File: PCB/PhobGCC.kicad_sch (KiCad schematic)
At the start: 46 parts, among them J1 Conn_01x06_Female, J2 Conn_01x04_Female, J3 Conn_01x01_Male, J4 Conn_01x01_Male, J6 10118194-0001LF, SW1 A, SW10 Dup, SW11 Dright, SW12 Ddown, SW2 B, SW3 X, SW4 Y, SW5 Start, SW6 L, SW7 R, SW8 1825027-5, SW9 Dleft, U1 Teensy3.2, U2 2x DRV5053CAQLPGM Hall Effect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, U3 2.5V LDO

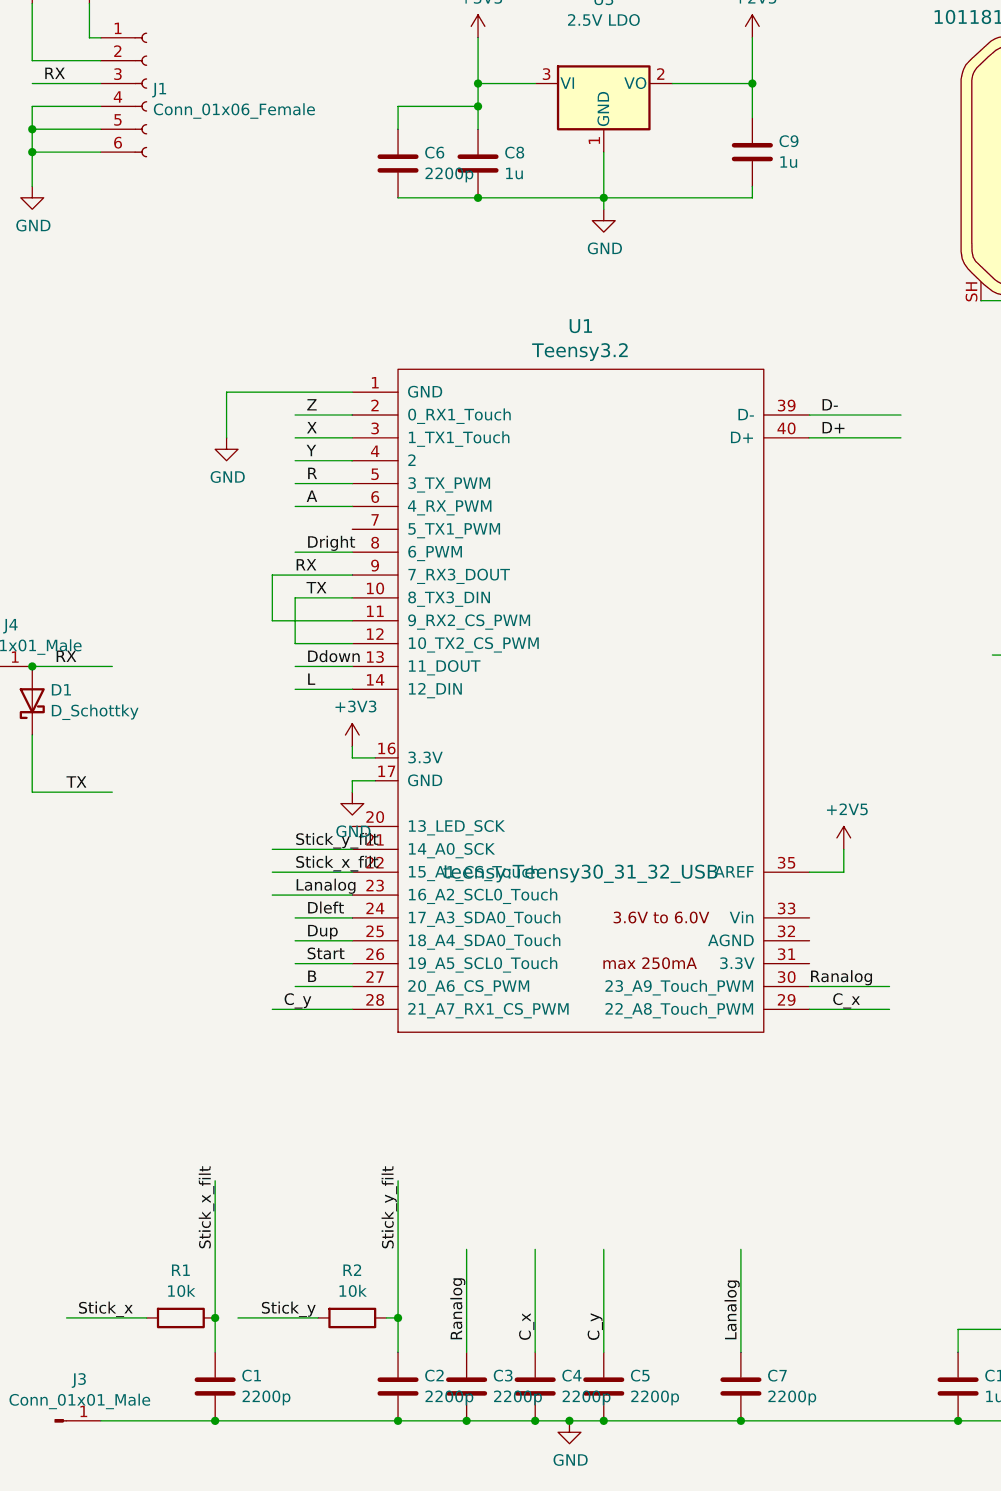
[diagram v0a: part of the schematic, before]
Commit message: Software tweaks to make the 1.1 version board work, and increasing the capacitors on the analog inputs
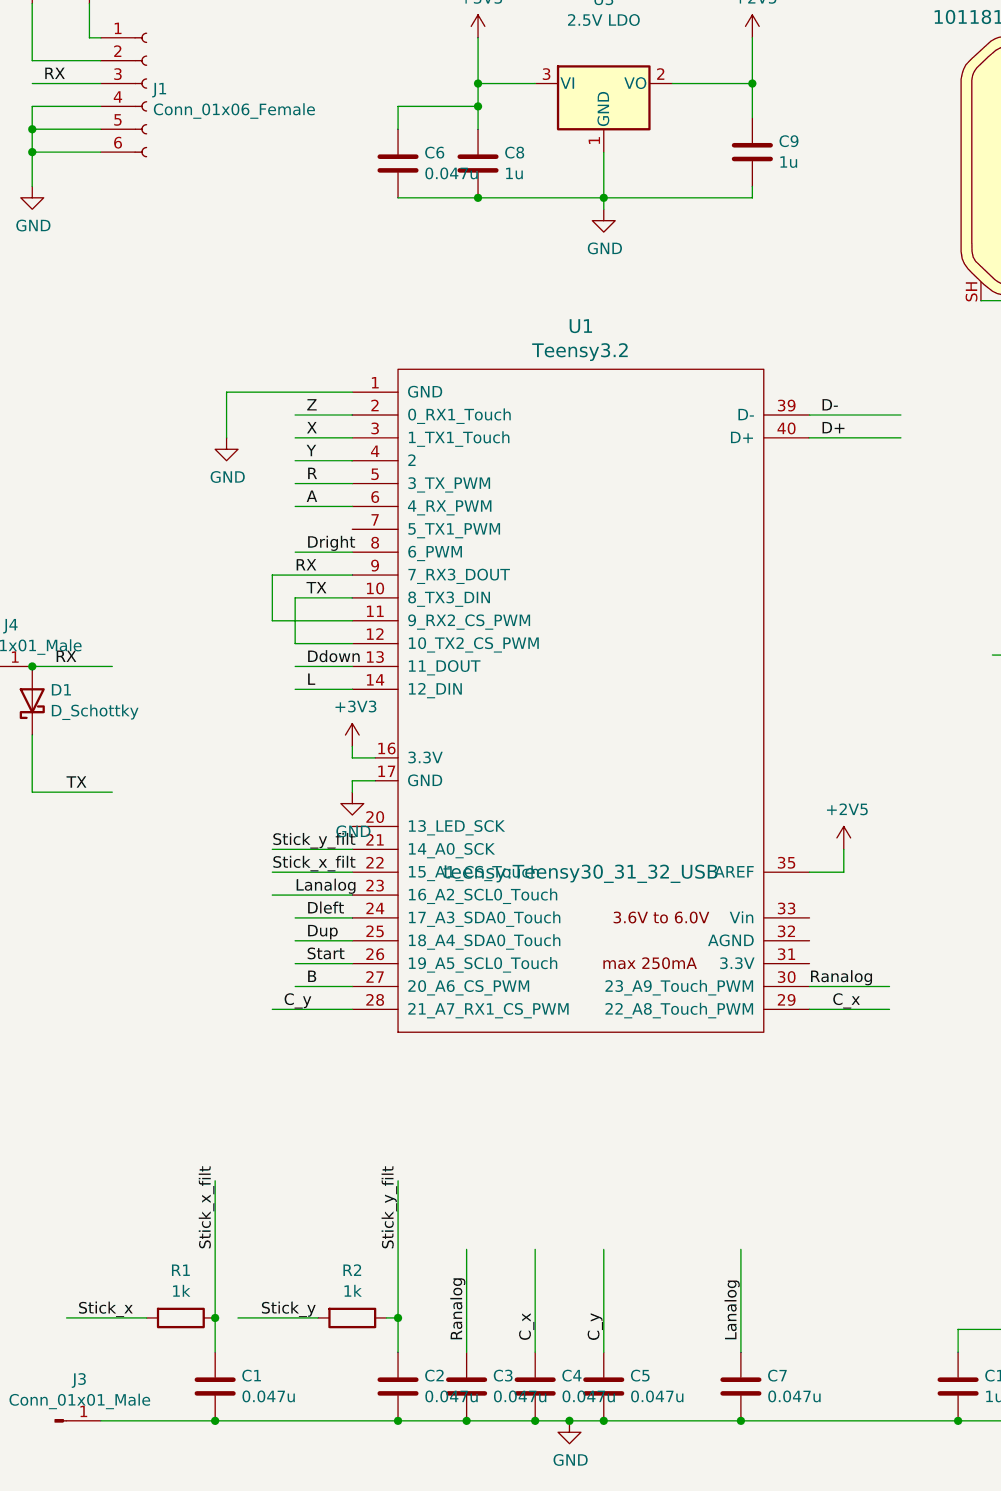
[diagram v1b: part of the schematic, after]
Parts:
- C1, C2, C3, C4, C5, C6, C7: value 2200p -> 0.047u; LCSC C1604 -> (none); MPN 0603B222K500NT -> (none); Manufacturer FH(Guangdong Fenghua Advanced Tech) -> (none)
- R1: value 10k -> 1k; LCSC C25804 -> (none); MPN 0603WAF1002T5E -> (none); Manufacturer UNI-ROYAL -> (none); Manufacturer PN 0603WAF1002T5ECopy -> (none)
- R2: value 10k -> 1k; LCSC C25804 -> (none); MPN 0603WAF1002T5E -> (none); Manufacturer UNI-ROYAL -> (none)

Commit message: Reverted the kicad and gerber files back to the 1.1 board version so they match up with the manufacturing files for JLC
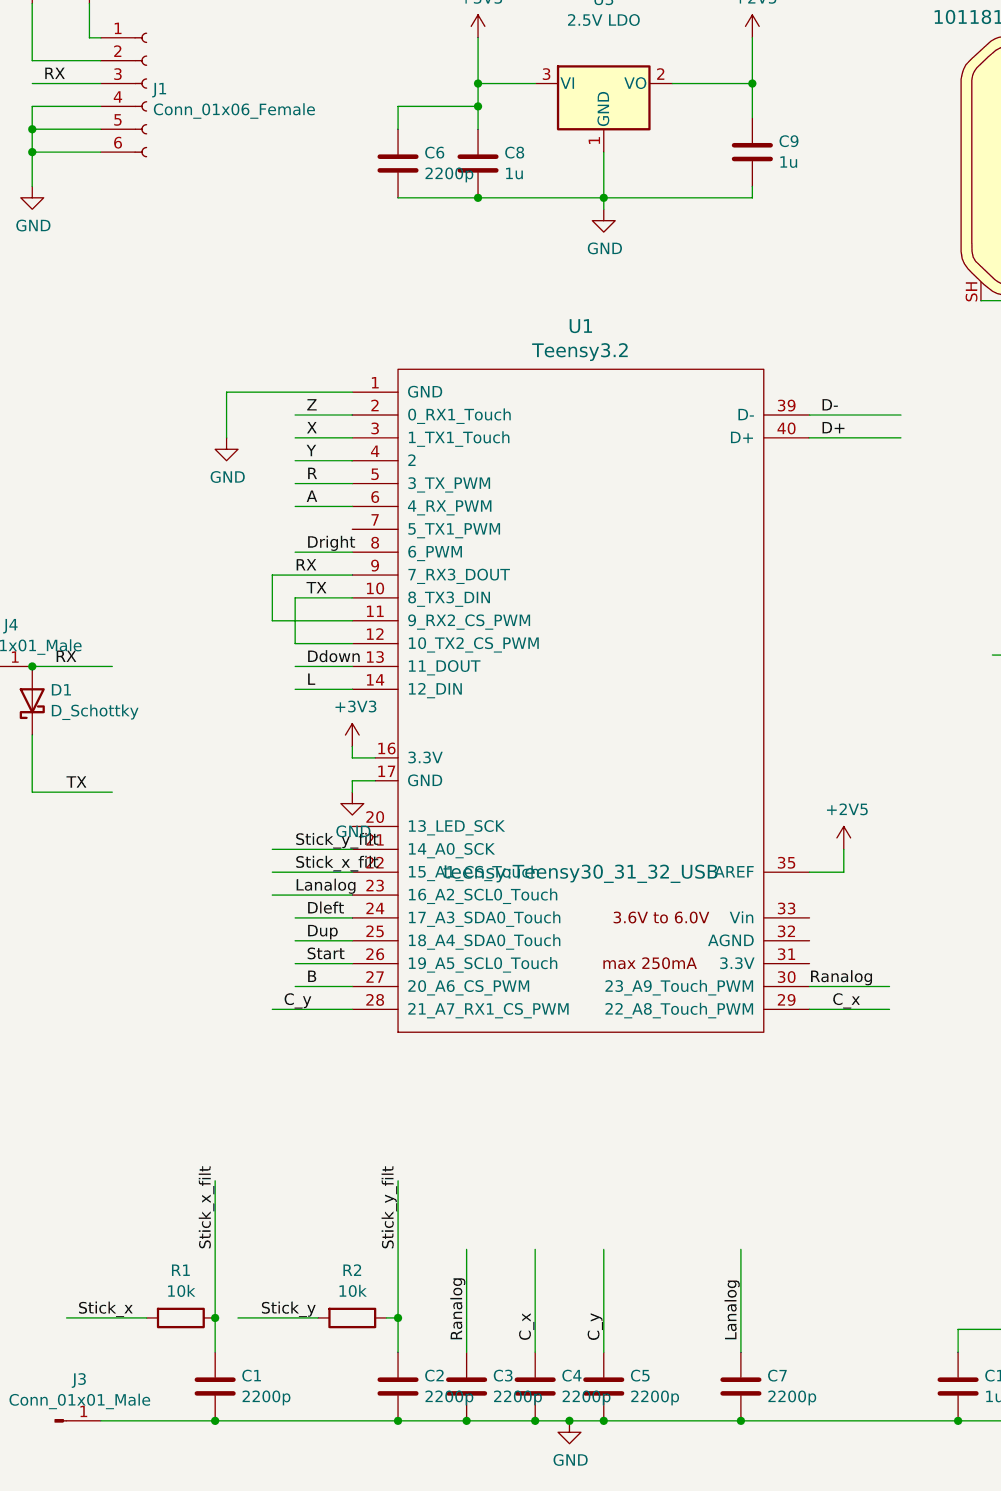
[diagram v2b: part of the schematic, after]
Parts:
- C1, C2, C3, C4, C5, C6, C7: value 0.047u -> 2200p; LCSC (none) -> C1604; MPN (none) -> 0603B222K500NT; Manufacturer (none) -> FH(Guangdong Fenghua Advanced Tech)
- R1: value 1k -> 10k; LCSC (none) -> C25804; MPN (none) -> 0603WAF1002T5E; Manufacturer (none) -> UNI-ROYAL; Manufacturer PN (none) -> 0603WAF1002T5ECopy
- R2: value 1k -> 10k; LCSC (none) -> C25804; MPN (none) -> 0603WAF1002T5E; Manufacturer (none) -> UNI-ROYAL
